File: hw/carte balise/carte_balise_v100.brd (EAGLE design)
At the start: 82.5 x 82.5 mm, 70 parts, among them IC1 DSPIC33EP512MU810-X_PF, IC2 MCP2551/SN, IC3 MRF24J40MAGND, IC4 MCP2551/SN, M3 DMP2035U, U1 ADXL362

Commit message: wip
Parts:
- moved UART1 110.6 mm to (41.9, 10.2)
- moved C10 97.2 mm to (28.3, 2.64), turned to 270 degrees
- moved C9 96.0 mm to (27.2, 4.01), turned to 270 degrees
- moved C11 95.8 mm to (26.3, 5.84), turned to 180 degrees
- moved C7 95.8 mm to (27.2, 0.99), turned to 270 degrees
- moved UART2 94.0 mm to (36.0, 10.0), turned to 180 degrees
- moved R16 90.7 mm to (20.8, -2.16), turned to 180 degrees
- moved U$3 90.2 mm to (20.7, -0.79), turned to 180 degrees
- moved C12 87.6 mm to (18.4, 0.64), turned to 90 degrees
- moved U$2 85.2 mm to (22.9, 2.54), turned to 90 degrees
- moved R17 69.9 mm to (-7.62, 8.89), turned to 180 degrees
- moved C14 68.2 mm to (-7.62, 7.62), turned to 180 degrees
- moved C13 66.5 mm to (-7.62, 6.35), turned to 180 degrees

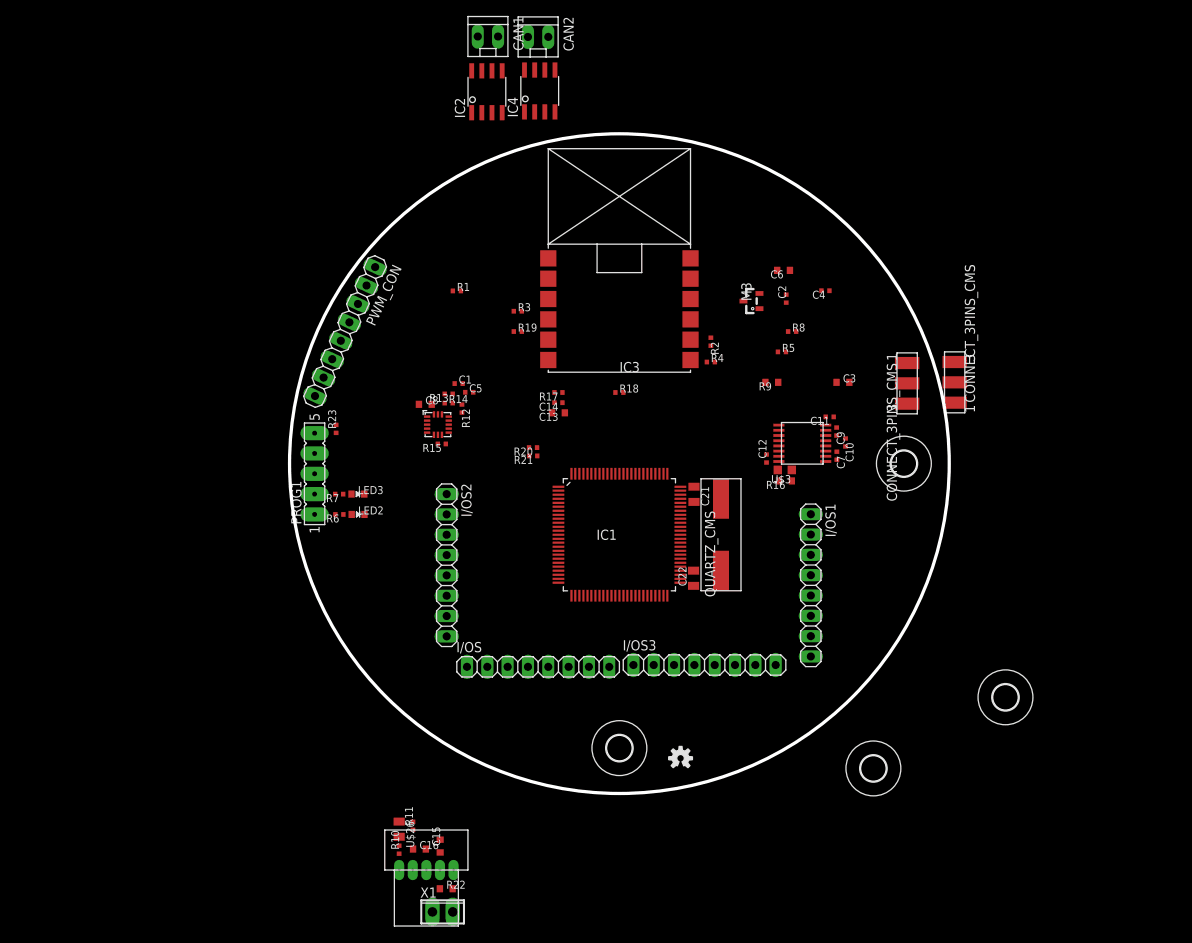
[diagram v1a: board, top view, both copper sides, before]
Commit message: rework io connector and start routing the board
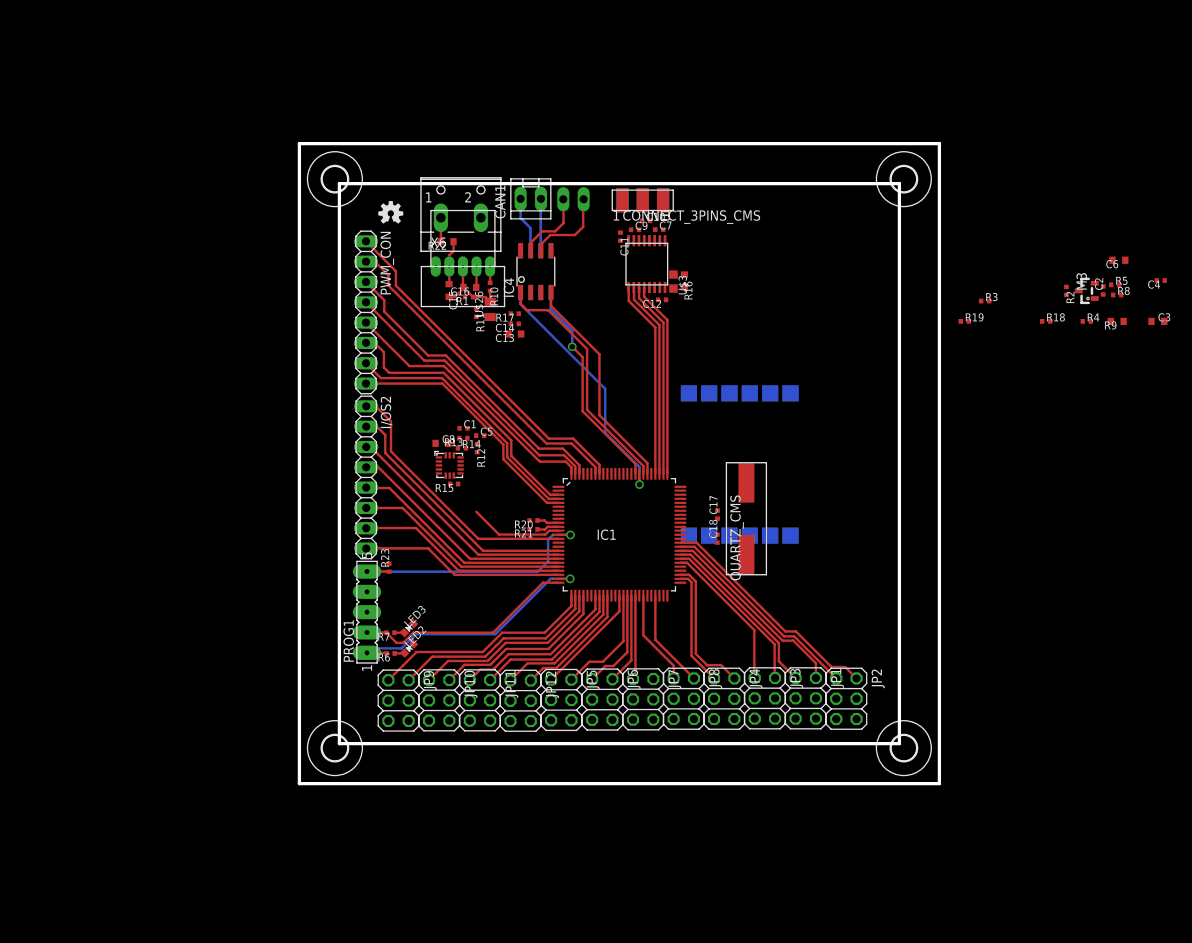
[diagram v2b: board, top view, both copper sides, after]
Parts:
- removed C21, C22: C_NP_805, etienne:805
- removed I/OS, I/OS1, I/OS3: (no value), pinhead-2:1X08
- removed X1: (no value), con-phoenix-254:2POL254
- added C17, C18: 22p-0402, DEVIALET_CAPACITORS:0402K
- added JP1, JP10, JP11, JP12, JP2, JP3, JP4, JP5, JP6, JP7, JP8, JP9: (no value), pinhead:2X03
- added X6: +12V, con-wago-500:W237-102
- moved R22 80.9 mm to (-21.5, 27.7), turned to 180 degrees
- moved H2 79.5 mm to (-35.6, 35.6)
- moved U$1 77.1 mm to (-28.6, 31.3)
- moved U$27 75.6 mm to (-19.6, 24.6), turned to 180 degrees
- moved R10 71.3 mm to (-16.2, 22.1), turned to 270 degrees
- moved C16 70.5 mm to (-18.7, 22.0), turned to 180 degrees
- moved C15 69.5 mm to (-21.3, 21.6), turned to 270 degrees
- moved H3 66.0 mm to (35.6, 35.6)
- moved U$26 66.0 mm to (-16.2, 19.3), turned to 90 degrees
- moved R11 64.6 mm to (-17.9, 18.8), turned to 270 degrees
- moved R3 58.4 mm to (45.7, 20.3)
- moved R19 55.9 mm to (43.2, 17.8)
- moved R18 54.1 mm to (53.3, 17.8)
- moved R4 47.3 mm to (58.4, 17.8)
- moved UART1 45.2 mm to (2.92, 32.9), flipped to the bottom, turned to 90 degrees
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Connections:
- net CAN1_RX: now also IC1.83; no longer IC1.84
- net CAN1_TX: now also IC1.84; no longer IC1.83
- net CAN2_RX: now also IC1.81; no longer IC1.82
- net CAN2_TX: now also IC1.82; no longer IC1.81
- net GND: now also C17.1, C18.1, JP1.3, JP1.4, JP10.3, JP10.4, JP11.3, JP11.4, JP12.3, JP12.4, JP2.3, JP2.4, JP3.3, JP3.4, JP4.3, JP4.4, JP5.3, JP5.4, JP6.3, JP6.4, JP7.3, JP7.4, JP8.3, JP8.4, JP9.3, JP9.4, X6.2; no longer C21.1, C22.1, X1.1
- net N$29: now also C18.2; no longer C22.2
- net N$30: now also C17.2; no longer C21.2
- net N$31: now also X6.1; no longer X1.2
- net PIC_RA1: now also JP5.1; no longer I/OS3.1
- net PIC_RA10: now also JP10.2; no longer I/OS.4
- net PIC_RA2: now also JP1.1; no longer I/OS1.4
- net PIC_RA3: now also JP1.2; no longer I/OS1.3
- net PIC_RA4: now also JP2.1; no longer I/OS1.2
- net PIC_RA5: now also JP2.2; no longer I/OS1.1
- net PIC_RA9: now also JP10.1; no longer I/OS.3
- net PIC_RB10: now also JP12.1; no longer I/OS.7
- net PIC_RB11: now also JP12.2; no longer I/OS.8
- net PIC_RB12: now also JP6.2; no longer I/OS3.4
- net PIC_RB13: now also JP7.1; no longer I/OS3.5
- net PIC_RB14: now also JP7.2; no longer I/OS3.6
- net PIC_RB15: now also JP8.1; no longer I/OS3.7
- net PIC_RB6: now also JP9.1; no longer I/OS.1
- net PIC_RB7: now also JP9.2; no longer I/OS.2
- net PIC_RB8: now also JP11.1; no longer I/OS.5
- net PIC_RB9: now also JP11.2; no longer I/OS.6
- net PIC_RD14: now also JP8.2; no longer I/OS3.8
- net PIC_RF12: now also JP6.1; no longer I/OS3.3
- net PIC_RF13: now also JP5.2; no longer I/OS3.2
- net PIC_RF2: now also JP4.1; no longer I/OS1.8
- net PIC_RF8: now also JP4.2; no longer I/OS1.7
- net PIC_RG2: now also JP3.2; no longer I/OS1.5
- net PIC_RG3: now also JP3.1; no longer I/OS1.6
- net UART1_RX: now also IC1.76; no longer IC1.77
- net UART1_TX: now also IC1.77; no longer IC1.76
- net V+: now also JP1.5, JP1.6, JP10.5, JP10.6, JP11.5, JP11.6, JP12.5, JP12.6, JP2.5, JP2.6, JP3.5, JP3.6, JP4.5, JP4.6, JP5.5, JP5.6, JP6.5, JP6.6, JP7.5, JP7.6, JP8.5, JP8.6, JP9.5, JP9.6
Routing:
- net PWM1_L: track 0.00 -> 42.9 mm
- net PWM1_H: track 0.00 -> 40.9 mm
- net PWM2_L: track 0.00 -> 38.1 mm
- net PWM2_H: track 0.00 -> 35.6 mm
- net PWM3_H: track 0.00 -> 34.2 mm
- net PWM3_L: track 0.00 -> 34.0 mm
- net !MCLR: track 0.00 -> 33.2 mm, vias 0 -> 1
- net PGEC/RX: track 0.00 -> 33.2 mm, vias 0 -> 1
- net PIC_RG9: track 0.00 -> 33.1 mm
- net PWM4_L: track 0.00 -> 32.1 mm
- net PIC_RA0: track 0.00 -> 31.8 mm
- net CAN1_RX: track 0.00 -> 31.5 mm, vias 0 -> 1
- net PWM4_H: track 0.00 -> 31.3 mm
- net CAN2_TX: track 0.00 -> 30.6 mm
- net PIC_RE8: track 0.00 -> 29.7 mm
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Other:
- board size 82.5 x 82.5 mm -> 80 x 80 mm

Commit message: wip routing and placement
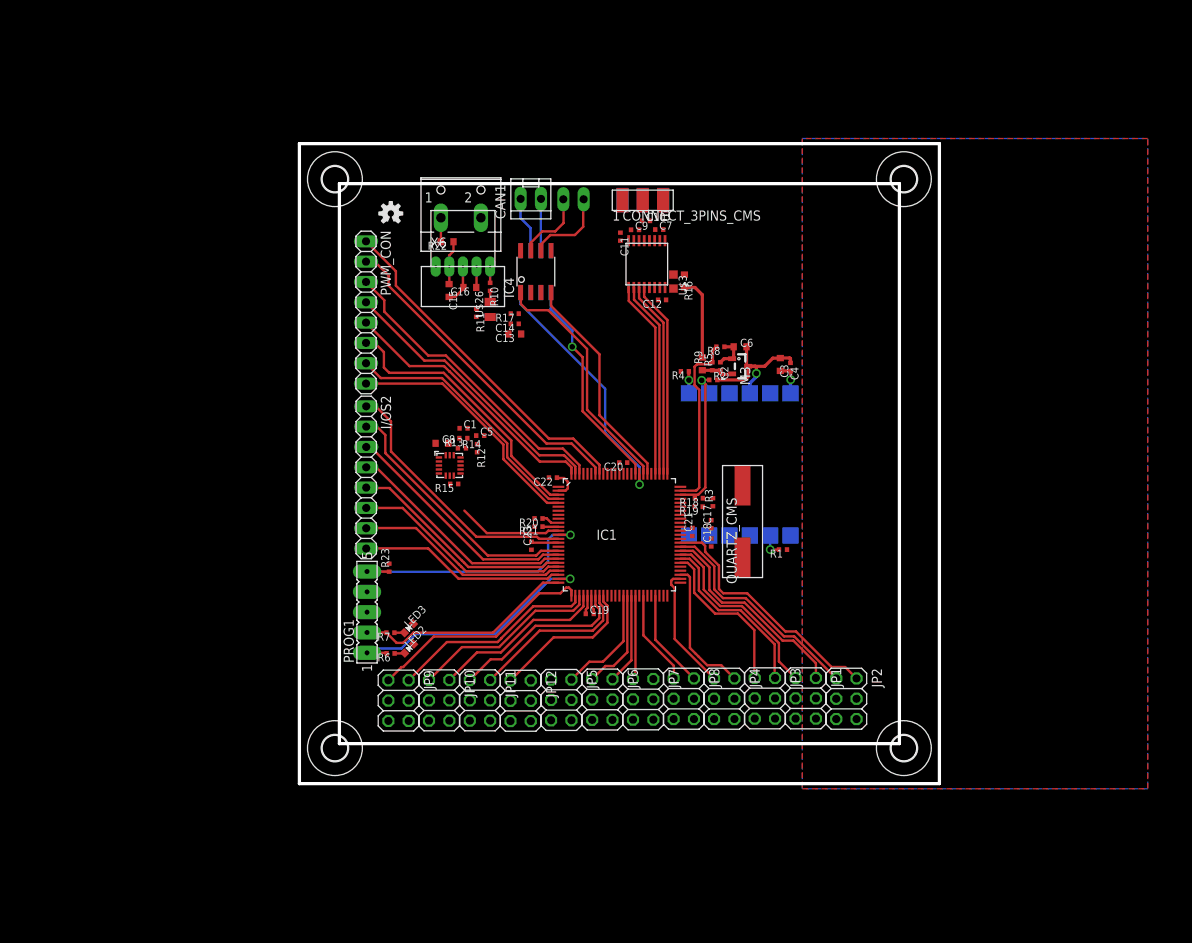
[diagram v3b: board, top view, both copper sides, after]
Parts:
- added C19, C20, C21, C22, C23: 100n-0402, DEVIALET_CAPACITORS:0402K
- moved R9 52.1 mm to (10.4, 12.5), turned to 90 degrees
- moved R5 51.4 mm to (11.6, 12.2), turned to 90 degrees
- moved R4 50.6 mm to (8.18, 11.5), turned to 180 degrees
- moved R1 50.4 mm to (20.4, -10.7)
- moved R8 50.0 mm to (12.6, 14.6), turned to 180 degrees
- moved C2 48.8 mm to (12.6, 12.2), turned to 270 degrees
- moved R18 48.7 mm to (9.93, -4.32), turned to 180 degrees
- moved C6 48.6 mm to (15.1, 14.6), turned to 0 degrees
- moved C4 47.5 mm to (21.4, 12.1), turned to 270 degrees
- moved C3 47.5 mm to (20.1, 12.4), turned to 270 degrees
- moved R2 45.5 mm to (11.7, 10.5), turned to 0 degrees
- moved M3 44.3 mm to (15.1, 12.2), turned to 270 degrees
- moved R3 42.3 mm to (11.7, -4.83), turned to 90 degrees
- moved R19 40.5 mm to (9.91, -5.38), turned to 180 degrees
- moved C17 1.43 mm to (11.5, -7.57)
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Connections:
- removed net +3V3P: R16.2, R9.2
- removed net N$10: R2.2, R3.2
- net +3V3: now also R16.2, R9.2; no longer R17.2
- net GND: now also C19.2, C20.2, C21.2, C22.2, C23.2
- net V+: now also C19.1, C20.1, C21.1, C22.1, C23.1, R17.2
- net VDD_RADIO: now also R2.2, R3.2
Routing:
- net !ZB_3V3_EN: track 0.00 -> 22.9 mm
- net !ZB_CS: track 0.00 -> 20.1 mm, vias 0 -> 1
- net VDD_RADIO: track 0.00 -> 18.8 mm, vias 0 -> 1
- net PIC_RB11: track 15.5 -> 0.00 mm
- net PIC_RA1: track 14.0 -> 0.00 mm
- net +3V3: track 2.63 -> 13.1 mm
- net GND: track 10.5 -> 17.0 mm, vias 0 -> 1
- net V+: track 0.00 -> 6.04 mm
- net N$1: track 0.00 -> 4.39 mm
- net N$2: track 0.00 -> 4.18 mm
- net N$7: track 0.00 -> 2.98 mm, vias 0 -> 1
- net !ZB_RESET: track 0.00 -> 2.85 mm, vias 0 -> 1
- net PIC_RA5: track 29.0 -> 31.2 mm
- net PIC_RG3: track 18.7 -> 20.5 mm
- net PIC_RA4: track 26.3 -> 28.0 mm
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- added copper zone on layer 1, net GND
- added copper zone on layer 16, net GND

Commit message: WIP adxl
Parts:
- removed R20: 33R-0402, DEVIALET_RESISTORS:0402K
- added R24: 33R-0402, DEVIALET_RESISTORS:0402K
- moved R14 10.3 mm to (-12.5, -5.51), turned to 180 degrees
- moved R15 7.62 mm to (-14.7, -7.24)
- moved U1 6.93 mm to (-15.2, -3.61)
- moved C8 6.75 mm to (-18.1, -2.84), turned to 90 degrees
- moved R13 6.09 mm to (-15.2, -1.09), turned to 0 degrees
- moved C1 5.88 mm to (-15.7, -0.08)
- moved C5 3.10 mm to (-17.3, 0.41), turned to 90 degrees
- moved R12 1.69 mm to (-16.2, 1.40)
- moved R21 1.03 mm to (-11.0, -7.39)
- moved C20 0.87 mm to (-0.38, 0.23)
- moved C19 0.32 mm to (-3.94, -19.0)
- moved JP8 0.23 mm to (8.05, -29.6)
- moved JP1 0.21 mm to (23.3, -29.5)
- moved JP3 0.21 mm to (18.2, -29.5)
- moved JP4 0.18 mm to (13.2, -29.6)
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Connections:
- removed net N$39: IC1.10, R20.1
- new net N$10: IC1.12, R24.1
- net !ADXL_CS: now also IC1.9; no longer IC1.7
- net +3V3: now also JP1.5, JP1.6, JP10.5, JP10.6, JP11.5, JP11.6, JP12.5, JP12.6, JP2.5, JP2.6, JP3.5, JP3.6, JP4.5, JP4.6, JP5.5, JP5.6, JP6.5, JP6.6, JP7.5, JP7.6, JP8.5, JP8.6, JP9.5, JP9.6
- net ADXL_INT1: now also IC1.6; no longer IC1.8
- net ADXL_INT2: now also IC1.7; no longer IC1.9
- net ADXL_MISO: now also IC1.10; no longer IC1.12
- net ADXL_SCLK: now also R24.2; no longer R20.2
- net V+: no longer JP1.5, JP1.6, JP10.5, JP10.6, JP11.5, JP11.6, JP12.5, JP12.6, JP2.5, JP2.6, JP3.5, JP3.6, JP4.5, JP4.6, JP5.5, JP5.6, JP6.5, JP6.6, JP7.5, JP7.6, JP8.5, JP8.6, JP9.5, JP9.6
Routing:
- net +3V3: track 13.1 -> 139.4 mm, vias 0 -> 2
- net N$4: track 0.00 -> 24.1 mm, vias 0 -> 2
- net PIC_RB11: track 0.00 -> 18.0 mm
- net GND: track 17.0 -> 34.3 mm, vias 1 -> 4
- net PIC_RA1: track 0.00 -> 16.1 mm
- net ADXL_SCLK: track 0.00 -> 9.68 mm
- net !ADXL_CS: track 0.00 -> 8.38 mm
- net ADXL_MOSI: track 0.00 -> 7.56 mm
- net V+: track 6.04 -> 13.3 mm
- net ADXL_INT1: track 0.00 -> 6.93 mm
- net ADXL_INT2: track 0.00 -> 6.73 mm
- net ADXL_MISO: track 13.1 -> 7.02 mm
- net N$10: track 0.00 -> 2.90 mm
- net N$5: track 0.00 -> 2.52 mm
- net N$39: track 1.42 -> 0.00 mm
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
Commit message: wip board
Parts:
- moved C11 7.37 mm to (7.49, 28.3)
- moved R17 3.79 mm to (-12.8, 15.0)
- moved C9 1.59 mm to (0.71, 28.2), turned to 270 degrees
- moved C7 1.00 mm to (5.87, 29.7)
- moved R16 0.94 mm to (9.07, 22.8)
- moved C10 0.83 mm to (3.86, 29.7)
- moved U$3 0.81 mm to (7.54, 22.9)
- moved U$2 0.66 mm to (4.09, 25.0)
- moved C12 0.55 mm to (5.87, 20.3)
- moved C14 0.31 mm to (-12.8, 17.4)
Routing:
- net V+: track 13.3 -> 59.8 mm, vias 0 -> 7
- net +3V3: track 139.4 -> 179.2 mm, vias 2 -> 4
- net GND: track 34.3 -> 60.4 mm, vias 4 -> 10
- net N$6: track 0.00 -> 11.5 mm, vias 0 -> 1
- net N$3: track 0.00 -> 11.0 mm, vias 0 -> 1
- net N$27: track 0.00 -> 7.41 mm
- net N$28: track 0.00 -> 5.53 mm
- net N$18: track 0.00 -> 4.43 mm
- net N$12: track 0.00 -> 4.14 mm
- net N$15: track 0.00 -> 3.54 mm
- net N$16: track 0.00 -> 2.00 mm
- net N$14: track 0.00 -> 1.95 mm
- net N$17: track 0.00 -> 1.85 mm
- net N$9: track 0.00 -> 1.83 mm
- net N$23: track 0.00 -> 1.73 mm
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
